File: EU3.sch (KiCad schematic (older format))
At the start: 54 parts, among them J301 ClockOut, J302 Doepfer connector, J303 ClockIn, J304 Out0, J305 Out1, J306 Out2, J307 Out3, J308 Out4, J309 Out5, J310 Out6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

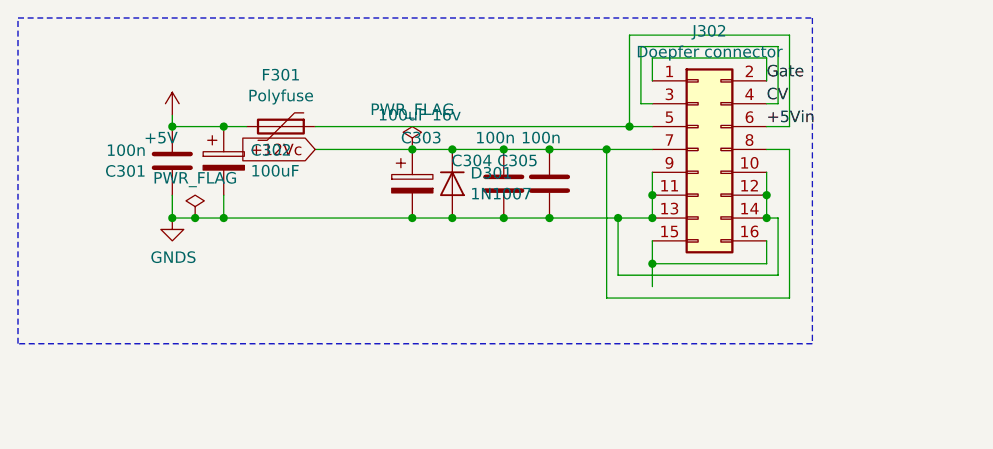
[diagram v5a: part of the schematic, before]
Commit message: Replace 16pin doepfer with 10pin on EU3
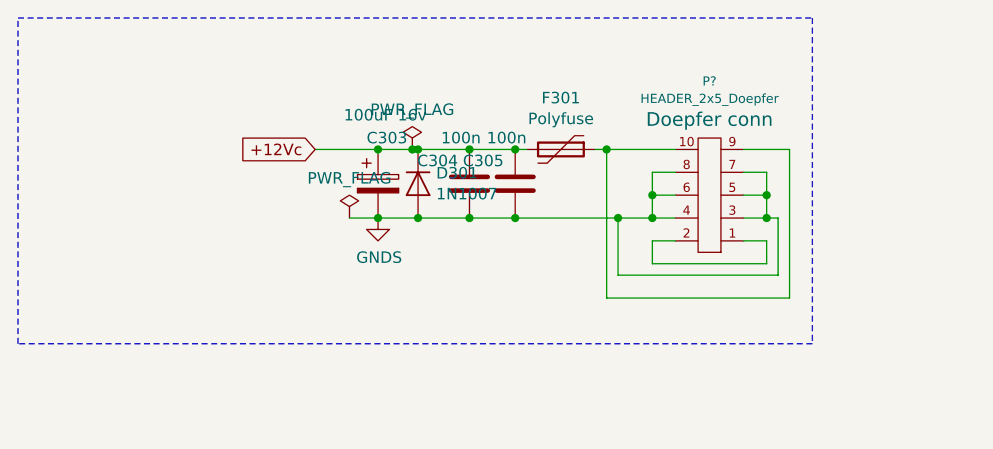
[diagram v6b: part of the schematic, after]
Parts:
- removed C301: 100n, Capacitor_SMD:C_0805_2012Metric_Pad1.15x1.40mm_HandSolder, symbol Device:C
- removed C302: 100uF, Capacitor_THT:CP_Radial_D5.0mm_P2.50mm, symbol Device:CP
- removed J302: Doepfer connector, Connector_PinSocket_2.54mm:PinSocket_2x08_P2.54mm_Vertical, symbol Connector_Generic:Conn_02x08_Odd_Even
- added P?: HEADER_2x5_Doepfer, Doepfer conn, symbol Eurorack:HEADER_2x5_Doepfer
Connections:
- net +5V is gone; now on net +12Vc: F301.2
- net GNDS: now also P?.3 (GND), P?.4 (GND), P?.5 (GND), P?.6 (GND), P?.7 (GND), P?.8 (GND)
- net +5Vin: no longer names the net of F301.1
- net +5Vin: now also P?.10 (+12), P?.9 (+12)
- new net: P?.1 (-12), P?.2 (-12)
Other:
- moved on the sheet: C303, C304, C305, D301, F301

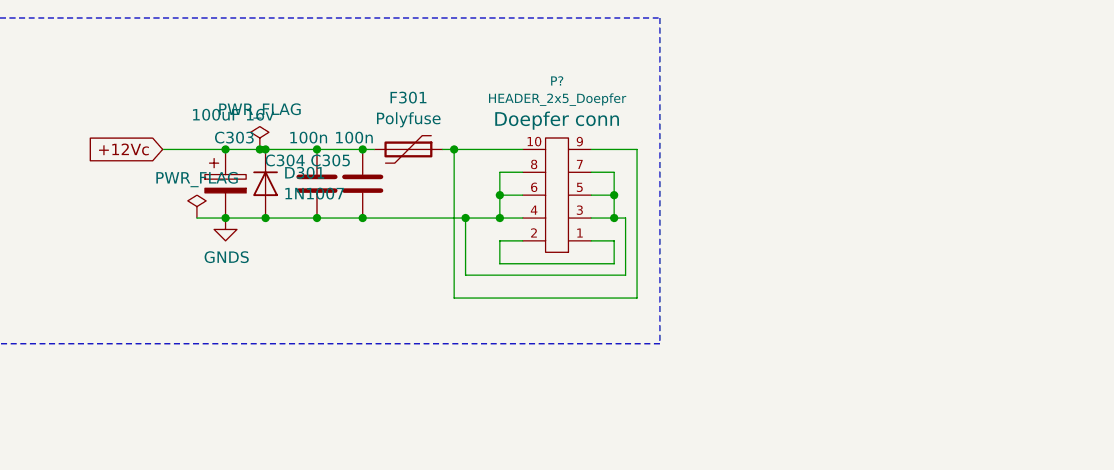
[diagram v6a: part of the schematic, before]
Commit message: EU3 placed and routed
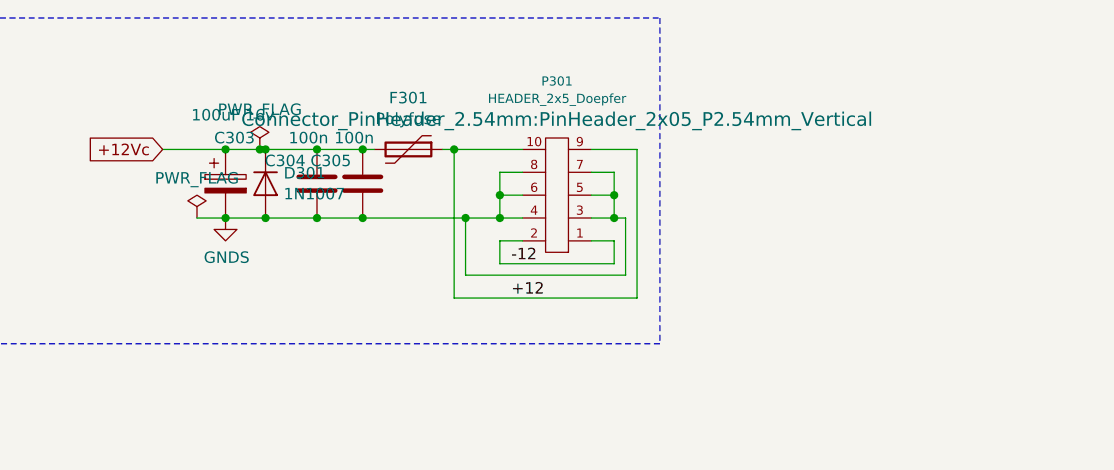
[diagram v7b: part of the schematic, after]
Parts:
- P301: renamed from P?; footprint Doepfer conn -> Connector_PinHeader_2.54mm:PinHeader_2x05_P2.54mm_Vertical
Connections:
- net +12: now reaches F301.1, P301.10 (+12), P301.9 (+12)
- net -12: now reaches P301.1 (-12), P301.2 (-12)
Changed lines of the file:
@@
 AR Path="/5C7FAEA2" Ref="P?"  Part="1"
 AR Path="/5D60ED9A/5C7FAEA2" Ref="P?"  Part="1"
-AR Path="/5C781441/5C7FAEA2" Ref="P?"  Part="1"
-F 0 "P?" H 3600 802 40  0000 C CNN
+AR Path="/5C781441/5C7FAEA2" Ref="P301"  Part="1"
+F 0 "P301" H 3600 802 40  0000 C CNN
 F 1 "HEADER_2x5_Doepfer" H 3600 878 40  0000 C CNN
-F 2 "Doepfer conn" H 3600 969 60  0000 C CNN
+F 2 "Connector_PinHeader_2.54mm:PinHeader_2x05_P2.54mm_Vertical" H 3600 969 60  0000 C CNN
 F 3 "" H 3600 1300 60  0000 C CNN
 	1    3600 1300
@@
 Wire Wire Line
 	3750 1100 3950 1100
+Text Label 3400 1600 0    50   ~ 0
+-12
+Text Label 3400 1750 0    50   ~ 0
++12
 $EndSCHEMATC
